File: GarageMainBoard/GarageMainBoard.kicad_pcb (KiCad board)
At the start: 2 copper layers, 33 parts, among them J1 Conn_01x02, J2 Barrel_Jack, J3 Conn_02x13_Odd_Even, J4 Front_Panel_Connector, J5 RJ45, J6 RJ45, Q1 IRLML6344, Q2 IRLML6344, Q3 IRLML6344, U1 AP1117-33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

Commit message: Main PCB
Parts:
- added MP1: MOUNTHOLE, KevinLib:TH-M3, F.Cu at (144.0, 125.8)
- added MP2: MOUNTHOLE, KevinLib:TH-M3, F.Cu at (107.7, 125.2)
- added MP3: MOUNTHOLE, KevinLib:TH-M3, F.Cu at (142.4, 70.5)
- added MP4: MOUNTHOLE, KevinLib:TH-M3, F.Cu at (101.2, 100.0)
- added REF**: Logo, KevinLib:Logo, F.Cu at (111.2, 106.1)
- BZ1: footprint Buzzers_Beepers:BUZZER -> Buzzers_Beepers:Buzzer_12x9.5RM7.6
- C1: value CP1 -> 220u; footprint Capacitors_THT:CP_Radial_D10.0mm_P2.50mm -> Capacitors_THT:CP_Radial_D6.3mm_P2.50mm
- moved J2 34.2 mm to (103.8, 70.0)
- moved C1 34.0 mm to (120.0, 74.9), turned to 90 degrees
- moved J5 33.5 mm to (98.0, 87.5)
- moved J6 33.5 mm to (98.0, 112.5)
- moved U3 31.4 mm to (109.3, 115.4)
- moved U2 30.6 mm to (109.0, 84.7), turned to 180 degrees
- moved C5 29.1 mm to (108.0, 100.0)
- moved R15 29.1 mm to (108.0, 96.0)
- moved U1 28.1 mm to (130.3, 75.2)
- moved C2 28.0 mm to (133.8, 82.5)
- moved C3 27.8 mm to (126.0, 82.5)
- moved BZ1 27.1 mm to (134.0, 121.9)
- moved Q1 26.4 mm to (120.5, 89.5)
- moved Q3 26.4 mm to (114.0, 89.5)
- moved R12 26.4 mm to (114.0, 96.0)
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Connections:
- U2 pad 1: /HOLD_B -> /HOLD_LED_-
- U2 pad 3: /HOLD_LED_- -> /HOLD_B
- U3 pad 1: +3V3 -> /OPEN_HALL
- U3 pad 3: /OPEN_HALL -> +3V3
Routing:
- net +5V: track 0.00 -> 140.7 mm, vias 0 -> 2
- net +3V3: track 0.00 -> 121.2 mm, vias 0 -> 4
- net /HOLD_B: track 0.00 -> 64.4 mm, vias 0 -> 2
- net /HOLD_LED_-: track 0.00 -> 55.9 mm
- net /CLOSE_HALL: track 0.00 -> 47.6 mm, vias 0 -> 2
- net /OPEN_HALL: track 0.00 -> 44.8 mm, vias 0 -> 2
- net /PIEZO: track 0.00 -> 39.5 mm
- net /G_DOOR: track 0.00 -> 38.8 mm, vias 0 -> 1
- net /LIGHT: track 0.00 -> 32.4 mm, vias 0 -> 1
- net /DOOR_B: track 0.00 -> 28.5 mm
- net Net-(BZ1-Pad2): track 0.00 -> 24.1 mm, vias 0 -> 1
- net /SDA: track 0.00 -> 15.1 mm
- net /MOSI: track 0.00 -> 13.2 mm
- net Net-(J3-Pad18): track 0.00 -> 11.1 mm, vias 0 -> 1
- net Net-(Q1-Pad1): track 0.00 -> 10.3 mm
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- added copper zone on B.Cu, net GND
- added copper zone on F.Cu, net GND
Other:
- board outline added: 61.2 x 65.1 mm
- net class Power added: clearance 0.3048, trace_width 0.3048, via_dia 0.6858, via_drill 0.3302
- board text added: "Kevin Kessler 2018"

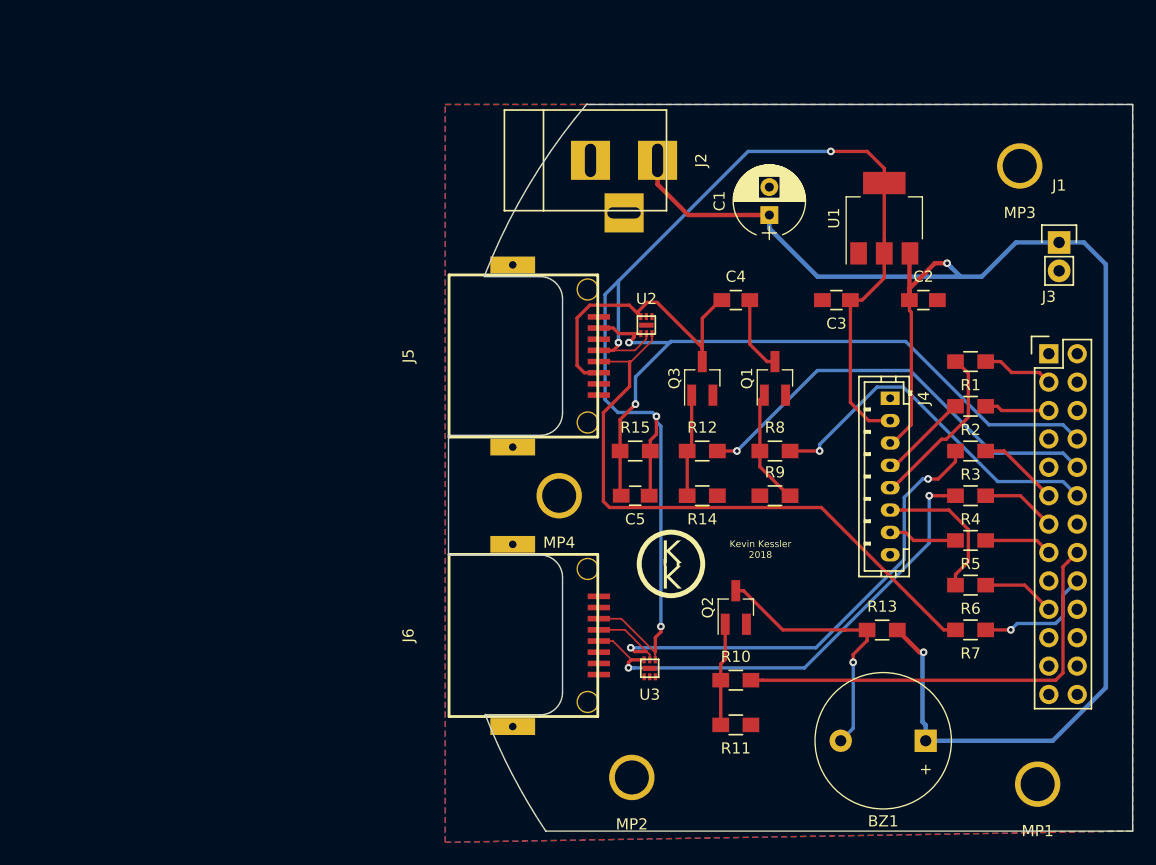
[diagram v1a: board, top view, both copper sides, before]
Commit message: Flip Main PCB
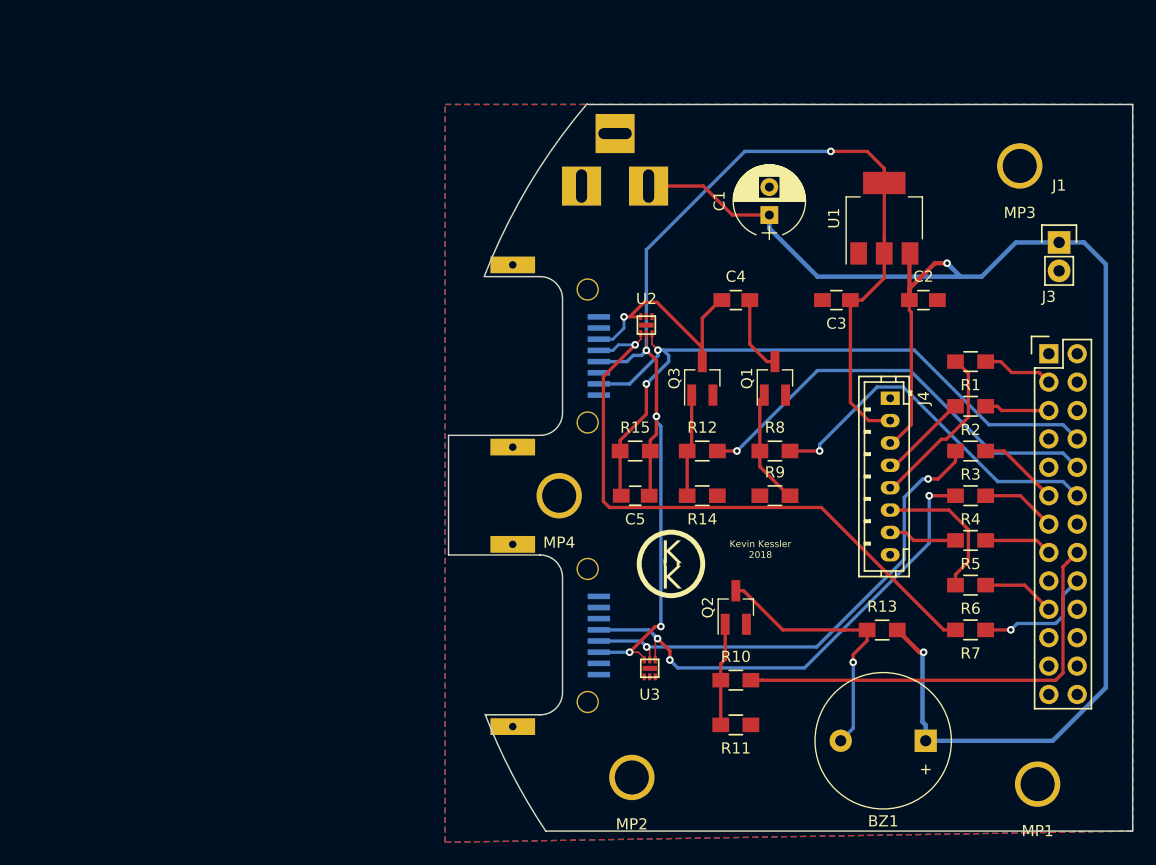
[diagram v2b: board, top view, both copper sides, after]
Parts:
- J2, J5, J6: moved to B.Cu
- moved J2 2.44 mm to (103.0, 72.3)
- turned J5 to 270 degrees
- turned J6 to 270 degrees
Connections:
- U2 pad 1: /HOLD_LED_- -> /HOLD_B
- U2 pad 3: /HOLD_B -> /HOLD_LED_-
- U3 pad 1: /OPEN_HALL -> +3V3
- U3 pad 3: +3V3 -> /OPEN_HALL
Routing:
- net +3V3: track 121.2 -> 108.5 mm, vias 4 -> 5
- net /DOOR_B: track 28.5 -> 21.4 mm, vias 0 -> 1
- net /CLOSE_HALL: track 47.6 -> 44.4 mm
- net +5V: track 140.7 -> 139.3 mm
- net /HOLD_LED_-: track 55.9 -> 56.1 mm, vias 0 -> 1
- net /OPEN_HALL: track 44.8 -> 44.6 mm, vias 2 -> 3

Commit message: Pull Ups on 365
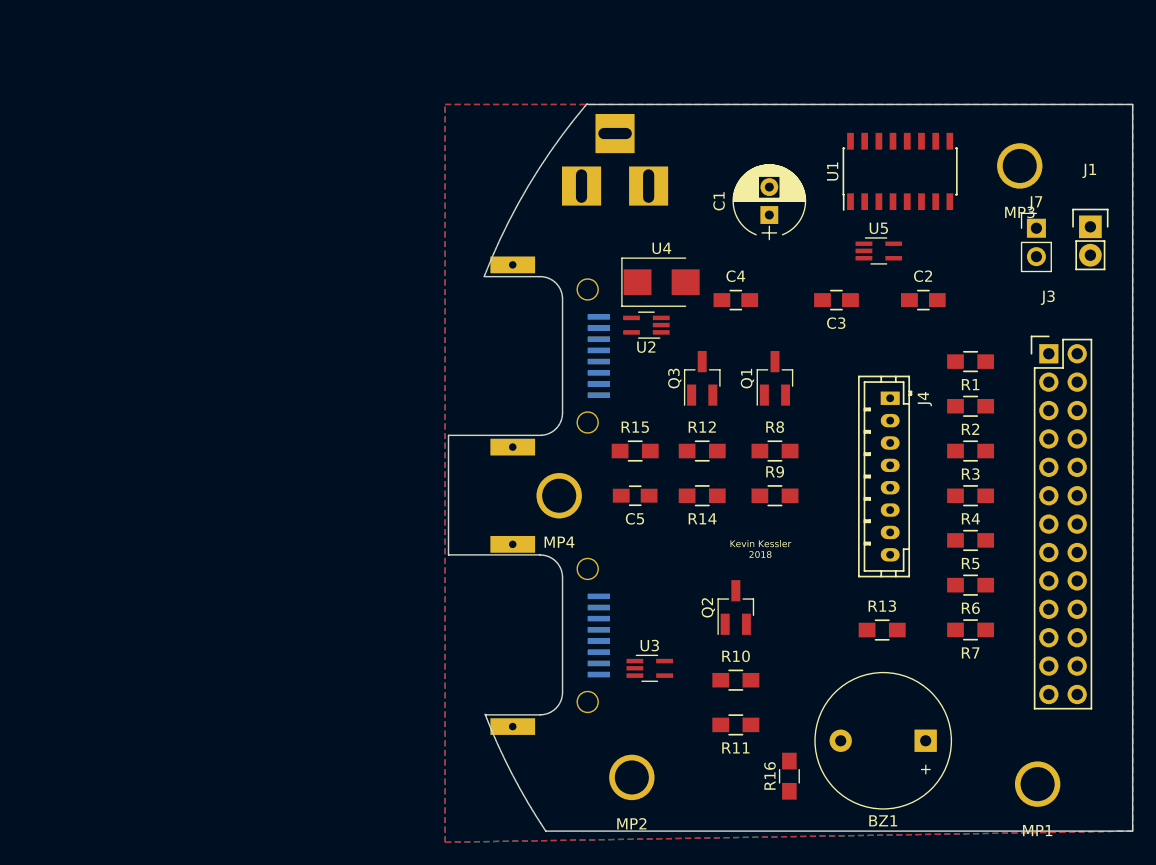
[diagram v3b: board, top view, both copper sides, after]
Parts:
- removed REF**: Logo, KevinLib:Logo
- added J7: 5V Jumper, Pin_Headers:Pin_Header_Straight_1x02_Pitch2.54mm, F.Cu at (143.9, 76.1)
- added R16: 1K, Resistors_SMD:R_0805_HandSoldering, F.Cu at (121.8, 125.1)
- added U4: TVS 20VDC, Diodes_SMD:D_SMB, F.Cu at (110.4, 80.9)
- added U5: MC74VHC1GT50, TO_SOT_Packages_SMD:SOT-353_SC-70-5_Handsoldering, F.Cu at (129.8, 78.1)
- C3: value 10u -> 100n
- C4: value 100u -> 1uF
- R5: value 100R -> 10K
- R6: value 100R -> 100
- R7: value 1OOR -> 1K
- U1: value AP1117-33 -> MC74HC365A; footprint TO_SOT_Packages_SMD:SOT-223-3Lead_TabPin2 -> Housings_SOIC:SOIC-16_3.9x9.9mm_Pitch1.27mm
- U2, U3: value uClamp3306 -> CPDV5-3V3UP; footprint KevinLibrary:SLP1616P6 -> TO_SOT_Packages_SMD:SOT-353_SC-70-5_Handsoldering
- moved U1 4.42 mm to (131.7, 71.0)
- moved J1 3.12 mm to (148.7, 75.9)
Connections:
- C2 pad 1: +5V -> GND
- C2 pad 2: GND -> +3V3
- C3 pad 1: +3V3 -> GND
- C3 pad 2: GND -> +5V
- J3 pad 1: (no net) -> +3V3
- J3 pad 15: Net-(J3-Pad15) -> /PIR_OUT
- J3 pad 18: Net-(J3-Pad18) -> /HOLD_LED
- J3 pad 19: Net-(J3-Pad19) -> /MOSI
- J3 pad 2: (no net) -> Net-(J3-Pad2)
- J3 pad 22: (no net) -> /ENABLE_1
- J3 pad 26: (no net) -> /ENABLE_2
- J3 pad 4: (no net) -> Net-(J3-Pad2)
- J4 pad 6: /MOSI -> Net-(J4-Pad6)
- J5 pad 4: +3V3 -> /HOLD_LED_+
- J5 pad 5: /HOLD_LED_- -> GND
- R10 pad 2: /PIEZO -> /PIEZO_X
- R12 pad 2: /G_DOOR -> /G_DOOR_X
- R5 pad 1: Net-(J3-Pad15) -> /PIR_OUT
- R5 pad 2: /PIR_OUT -> +3V3
- R6 pad 1: Net-(J3-Pad19) -> /HOLD_LED_+
- R6 pad 2: /MOSI -> /HOLD_LED_X
- R7 pad 1: Net-(J3-Pad18) -> /ENABLE_1
- R7 pad 2: /HOLD_LED_- -> +3V3
- R8 pad 2: /LIGHT -> /LIGHT_X
- U1 pad 1: GND -> /ENABLE_1
- U1 pad 2: +3V3 -> /LIGHT
- U1 pad 3: +5V -> /LIGHT_X
- U2 pad 2: +3V3 -> GND
- U2 pad 3: /HOLD_LED_- -> /HOLD_LED_+
- U2 pad 4: /DOOR_B -> (no net)
- U3 pad 2: /CLOSE_HALL -> GND
- U3 pad 3: /OPEN_HALL -> /CLOSE_HALL
- U3 pad 4: (no net) -> /OPEN_HALL
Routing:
- net +5V: track 139.3 -> 0.00 mm, vias 2 -> 0
- net +3V3: track 108.5 -> 0.00 mm, vias 5 -> 0
- net /HOLD_B: track 64.4 -> 0.00 mm, vias 2 -> 0
- net /HOLD_LED_-: track 56.1 -> 0.00 mm, vias 1 -> 0
- net /OPEN_HALL: track 44.6 -> 0.00 mm, vias 3 -> 0
- net /CLOSE_HALL: track 44.4 -> 0.00 mm, vias 2 -> 0
- net /PIEZO: track 39.5 -> 0.00 mm
- net /G_DOOR: track 38.8 -> 0.00 mm, vias 1 -> 0
- net /LIGHT: track 32.4 -> 0.00 mm, vias 1 -> 0
- net Net-(BZ1-Pad2): track 24.1 -> 0.00 mm, vias 1 -> 0
- net /DOOR_B: track 21.4 -> 0.00 mm, vias 1 -> 0
- net /SDA: track 15.1 -> 0.00 mm
- net /MOSI: track 13.2 -> 0.00 mm
- net Net-(J3-Pad18): track 11.1 -> 0.00 mm, vias 1 -> 0
- net Net-(Q1-Pad1): track 10.3 -> 0.00 mm
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
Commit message: PCB V2
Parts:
- added REF**: VIA_13MIL, KevinLib:VIA_13MIL, F.Cu at (133.3, 88.2)
- added REF**: VIA_13MIL, KevinLib:VIA_13MIL, F.Cu at (132.9, 69.5)
- added REF**: VIA_13MIL, KevinLib:VIA_13MIL, F.Cu at (136.2, 86.3)
- added REF**: VIA_13MIL, KevinLib:VIA_13MIL, F.Cu at (128.2, 85.4)
- J1: footprint Pin_Headers:Pin_Header_Straight_1x02 -> Pin_Headers:Pin_Header_Straight_1x02_Pitch2.54mm
- J3: footprint Pin_Headers:Pin_Header_Straight_2x13 -> Pin_Headers:Pin_Header_Straight_2x13_Pitch2.54mm
- moved R16 49.7 mm to (123.8, 75.4), turned to 270 degrees
- moved R6 40.9 mm to (123.8, 69.6), turned to 90 degrees
- moved R7 29.2 mm to (136.4, 82.8), turned to 270 degrees
- moved C2 8.79 mm to (125.1, 83.8), turned to 90 degrees
- moved U2 6.75 mm to (108.2, 91.4), turned to 270 degrees
- moved C1 6.09 mm to (116.1, 70.2), turned to 270 degrees
- moved C3 5.95 mm to (130.2, 86.7)
- moved U5 5.59 mm to (130.0, 83.7)
- moved R1 4.84 mm to (138.0, 92.8)
- moved U1 4.81 mm to (130.2, 75.6), turned to 180 degrees
- moved R2 4.14 mm to (138.0, 96.1)
- moved R3 3.95 mm to (138.0, 99.9)
- moved R4 3.12 mm to (138.0, 103.1)
- moved U3 2.82 mm to (109.0, 118.2), turned to 270 degrees
- moved R5 2.55 mm to (137.9, 106.6)
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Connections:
- U1 pad 2: /LIGHT -> /G_DOOR
- U1 pad 3: /LIGHT_X -> /G_DOOR_X
- U1 pad 4: /G_DOOR -> /LIGHT
- U1 pad 5: /G_DOOR_X -> /LIGHT_X
- U3 pad 1: +3V3 -> /CLOSE_HALL
- U3 pad 3: /CLOSE_HALL -> +3V3
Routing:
- net +3V3: track 0.00 -> 153.4 mm, vias 0 -> 4
- net +5V: track 0.00 -> 121.2 mm, vias 0 -> 3
- net /ENABLE_2: track 0.00 -> 76.0 mm, vias 0 -> 2
- net /HOLD_B: track 0.00 -> 59.1 mm, vias 0 -> 4
- net /HOLD_LED: track 0.00 -> 57.2 mm
- net /PIEZO_X: track 0.00 -> 54.5 mm, vias 0 -> 2
- net /MOSI: track 0.00 -> 53.2 mm
- net /OPEN_HALL: track 0.00 -> 51.0 mm, vias 0 -> 3
- net /ENABLE_1: track 0.00 -> 49.5 mm, vias 0 -> 2
- net /CLOSE_HALL: track 0.00 -> 48.7 mm, vias 0 -> 3
- net /PIEZO: track 0.00 -> 41.9 mm
- net /LIGHT: track 0.00 -> 34.9 mm
- net /G_DOOR_X: track 0.00 -> 32.0 mm, vias 0 -> 2
- net /HOLD_LED_+: track 0.00 -> 31.6 mm, vias 0 -> 1
- net /G_DOOR: track 0.00 -> 30.5 mm
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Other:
- net class 0.2mm: clearance 0.2 -> 0.2032; trace_width 0.2 -> 0.2032
- board text added: "Garage Server Main Board V2"
